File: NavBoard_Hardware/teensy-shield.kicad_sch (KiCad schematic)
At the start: 3 parts, among them J4 Teensy-2.54mm_Adapter, J5 Teensy Ethernet, U5 Teensy4.1

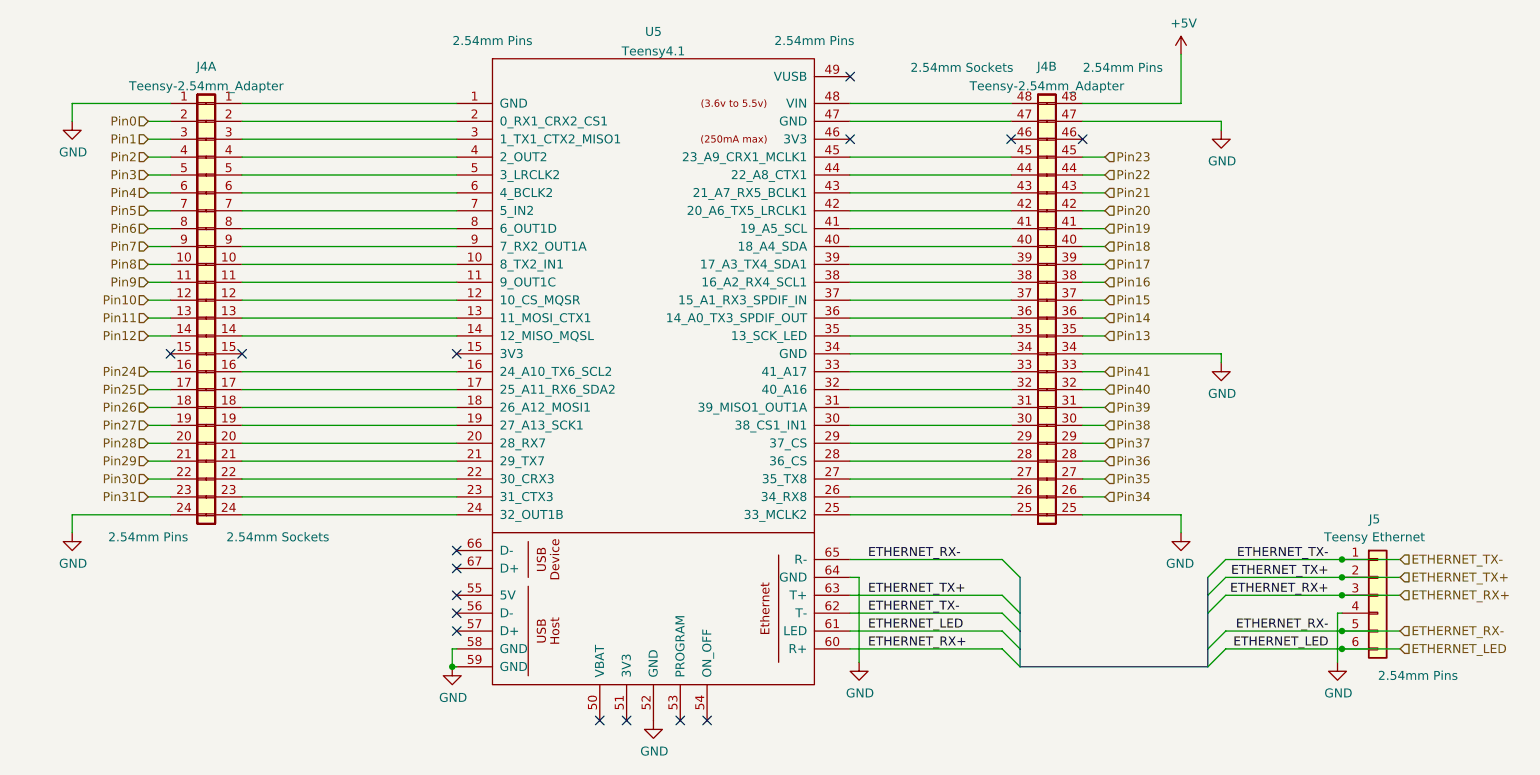
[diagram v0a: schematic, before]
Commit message: Completed routing, added 3D models to IMUs
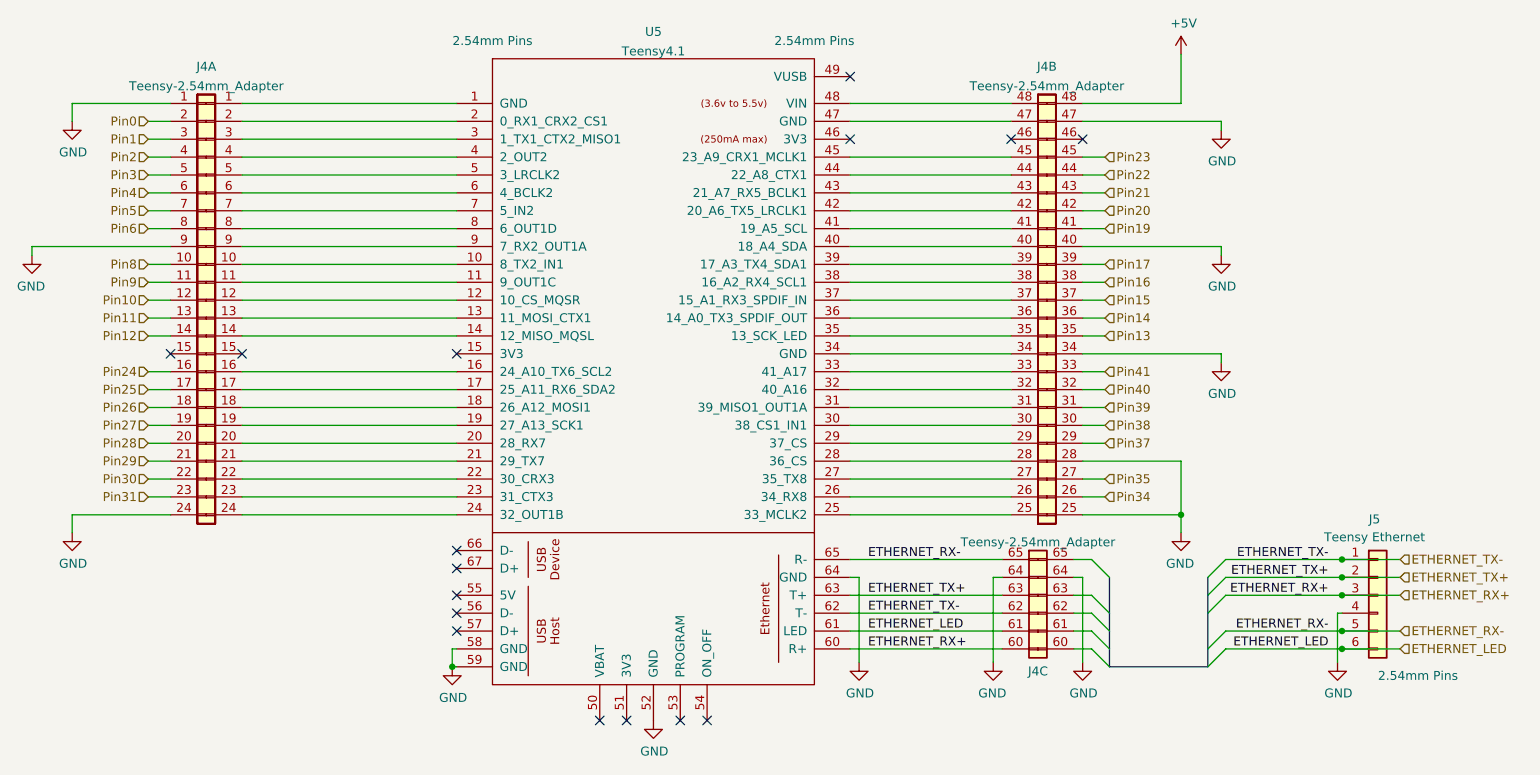
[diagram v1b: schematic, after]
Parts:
- added unit 3 of J4
- J4: Inner Type 2.54mm Sockets -> (none); Outer Types 2.54mm Pins -> (none)
- J4: Inner Type 2.54mm Sockets -> (none); Outer Type 2.54mm Pins -> (none)
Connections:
- net Pin18 is gone; now on net GND: J4.40
- net Pin36 is gone; now on net GND: J4.28
- net Pin7 is gone; now on net GND: J4.9
- net ETHERNET_LED: now also J4.61
- net ETHERNET_RX+: now also J4.60
- net ETHERNET_RX-: now also J4.65
- net ETHERNET_TX+: now also J4.63
- net ETHERNET_TX-: now also J4.62
- net GND: now also J4.64

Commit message: Annotated schematic pages
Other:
- company: (none) -> Thomas Francois, Missouri S&T Mars Rover Design Team
- title: (none) -> MRDT NavBoard - Teensy Adapter
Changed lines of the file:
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@@
 (kicad_sch (version 20211123) (generator eeschema)
   (paper "A4")
+  (title_block
+    (title "MRDT NavBoard - Teensy Adapter")
+    (rev "1, 2023")
+    (company "Thomas Francois, Missouri S&T Mars Rover Design Team")
+    (comment 1 "Teensy 4.1 and Adapter Board")
+    (comment 2 "Widens the Teensy to fit the other modules")
+  )
   (junction (at 247.015 127.635) (diameter 0) (color 0 0 0 0)
   )

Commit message: Initial changes and prototyping the new layout
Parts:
- removed U5: Teensy4.1, teensy:Teensy41, symbol teensy:Teensy4.1
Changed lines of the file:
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@@
     (pin "1")
-  )
-  (symbol (lib_id "teensy:Teensy4.1") (at 149.225 104.775 0) (unit 1)
-    (in_bom yes) (on_board yes)
-    (property "Reference" "U5" (id 0) (at 149.225 39.9755 0))
-    (property "Value" "Teensy4.1" (id 1) (at 149.225 42.7506 0))
-    (property "Footprint" "teensy:Teensy41" (id 2) (at 139.065 94.615 0)
-      (effects (font (size 1.27 1.27)) hide)
-    )
-    (property "Datasheet" "https://www.pjrc.com/store/teensy41.html" (id 3) (at 139.065 94.615 0)
-      (effects (font (size 1.27 1.27)) hide)
-    )
-    (property "Left Headers" "2.54mm Pins" (id 4) (at 126.365 41.275 0))
-    (property "Right Headers" "2.54mm Pins" (id 5) (at 172.085 41.275 0))
-    (pin "10")
-    (pin "11")
-    (pin "12")
-    (pin "13")
-    (pin "14")
-    (pin "15")
-    (pin "16")
-    (pin "17")
-    (pin "18")
-    (pin "19")
-    (pin "20")
-    (pin "21")
-    (pin "22")
-    (pin "23")
-    (pin "24")
-    (pin "25")
-    (pin "26")
-    (pin "27")
-    (pin "28")
-    (pin "29")
-    (pin "30")
-    (pin "31")
-    (pin "32")
-    (pin "33")
-    (pin "35")
-    (pin "36")
-    (pin "37")
-    (pin "38")
-    (pin "39")
-    (pin "40")
-    (pin "41")
-    (pin "42")
-    (pin "43")
-    (pin "44")
-    (pin "45")
-    (pin "46")
-    (pin "47")
-    (pin "48")
-    (pin "49")
-    (pin "5")
-    (pin "50")
-    (pin "51")
-    (pin "52")
-    (pin "53")
-    (pin "54")
-    (pin "55")
-    (pin "56")
-    (pin "57")
-    (pin "58")
-    (pin "59")
-    (pin "6")
-    (pin "60")
-    (pin "61")
-    (pin "62")
-    (pin "63")
-    (pin "64")
-    (pin "65")
-    (pin "66")
-    (pin "67")
-    (pin "7")
-    (pin "8")
-    (pin "9")
-    (pin "1")
-    (pin "2")
-    (pin "3")
-    (pin "34")
-    (pin "4")
   )
   (symbol (lib_id "Nav_Board:Teensy-2.54mm_Adapter") (at 203.835 113.665 0) (unit 3)
